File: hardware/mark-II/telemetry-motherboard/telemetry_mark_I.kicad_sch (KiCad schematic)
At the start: 78 parts, among them J1 Power, J10 5V_BUS, J11 12V_BUS, J12 24V_BUS, J13 Conn_01x02_Socket, J14 Conn_01x02_Socket, J15 Conn_01x02_Socket, J16 Conn_01x02_Socket, J17 BMS_Header, J2 PWM, J3 Analog, J4 PWM, J5 Analog, J6 Communication, J7 Digital, J8 Input_Terminal, J9 Temp_Sensor_Header, U3 LTC3114EFE-1_PBF, U4 AOZ1284PI, U5 AOZ1284PI

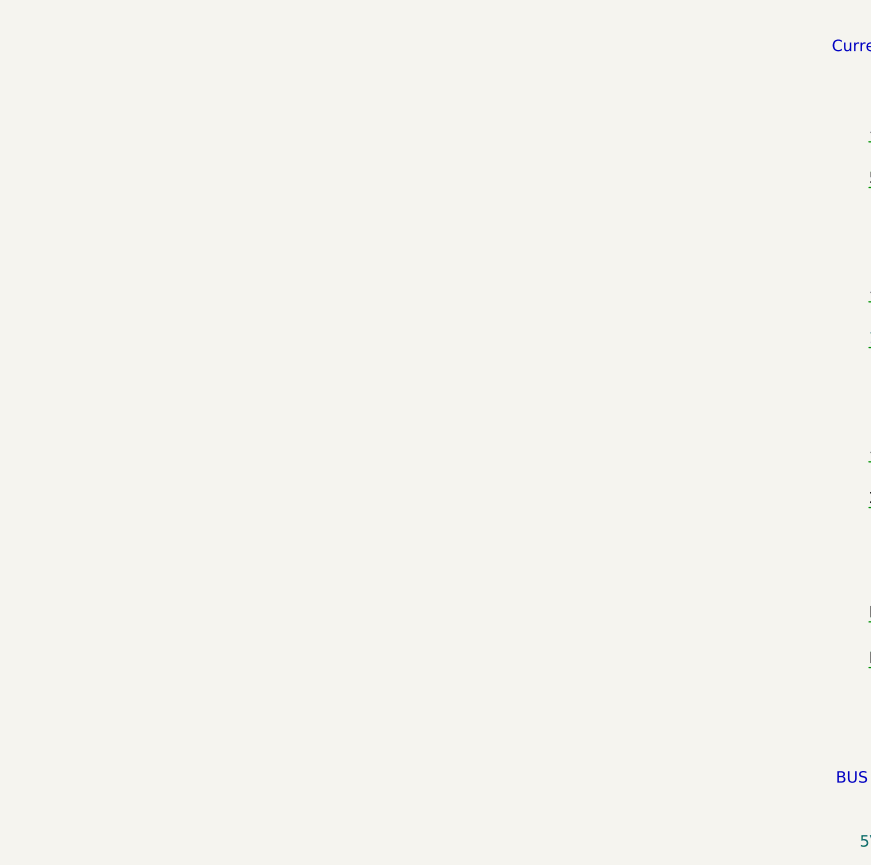
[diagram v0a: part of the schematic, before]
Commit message: Work on fault abstraction
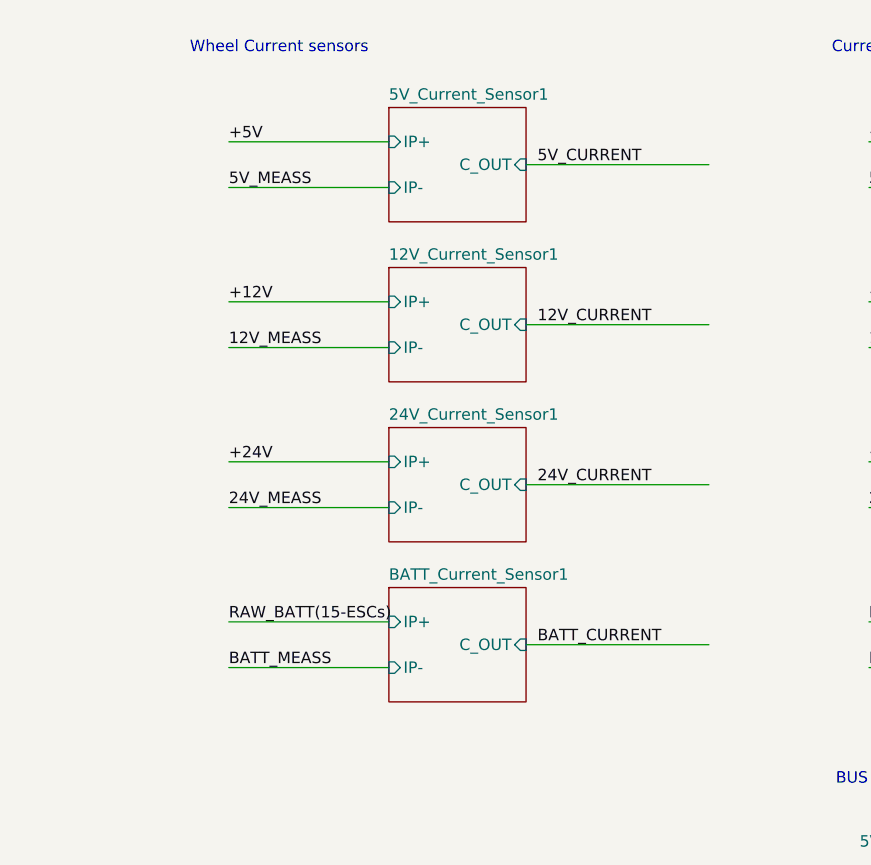
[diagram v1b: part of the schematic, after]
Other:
- added sheet 12V_Current_Sensor1 (current_sensor.kicad_sch)
- added sheet 24V_Current_Sensor1 (current_sensor.kicad_sch)
- added sheet 5V_Current_Sensor1 (current_sensor.kicad_sch)
- added sheet BATT_Current_Sensor1 (current_sensor.kicad_sch)
- note added: "Wheel Current sensors"

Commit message: New commit
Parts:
- removed C11: 30u, Capacitor_THT:CP_Radial_D5.0mm_P2.00mm, symbol Device:C_Polarized_Small_US
- removed C12, C17, C19, C27, C28: 10u, Capacitor_SMD:C_0603_1608Metric_Pad1.08x0.95mm_HandSolder, symbol Device:C_Small
- removed C14: 4.7n, Capacitor_SMD:C_0603_1608Metric_Pad1.08x0.95mm_HandSolder, symbol Device:C_Small
- removed C18, C20: 0.3n, Capacitor_SMD:C_0603_1608Metric_Pad1.08x0.95mm_HandSolder, symbol Device:C_Small
- removed C22, C23: 1n, Capacitor_SMD:C_0603_1608Metric_Pad1.08x0.95mm_HandSolder, symbol Device:C_Small
- removed C24, C25: 100n, Capacitor_SMD:C_0603_1608Metric_Pad1.08x0.95mm_HandSolder, symbol Device:C_Small
- removed C5, C6: 68n, Capacitor_SMD:C_0603_1608Metric_Pad1.08x0.95mm_HandSolder, symbol Device:C_Small
- removed C7: 33n, Capacitor_SMD:C_0603_1608Metric_Pad1.08x0.95mm_HandSolder, symbol Device:C_Small
- removed C9: 4.7u, Capacitor_SMD:C_0603_1608Metric_Pad1.08x0.95mm_HandSolder, symbol Device:C_Small
- removed D6, D7: SS54, Diode_SMD:D_SMA, symbol Device:D_Schottky
- removed J8: Input_Terminal, TerminalBlock_Ningbo-Kagnex:TerminalBlock_Ningbo-Kagnex_HB9500_1x05_P9.5mm, symbol Connector:Screw_Terminal_01x04
- removed L1: 6.8u, Inductor_SMD:L_0603_1608Metric_Pad1.05x0.95mm_HandSolder, symbol Device:L_Small
- removed L2, L3: 22u, Inductor_SMD:L_12x12mm_H8mm, symbol Device:L_Small
- removed R13: 27.4k, Resistor_SMD:R_0603_1608Metric_Pad0.98x0.95mm_HandSolder, symbol Device:R_Small_US
- removed R15: 43.2k, Resistor_SMD:R_0603_1608Metric_Pad0.98x0.95mm_HandSolder, symbol Device:R_Small_US
- removed R16, R26: 105k, Resistor_SMD:R_0603_1608Metric_Pad0.98x0.95mm_HandSolder, symbol Device:R_Small_US
- removed R17, R18: 47k, Resistor_SMD:R_0603_1608Metric_Pad0.98x0.95mm_HandSolder, symbol Device:R_Small_US
- removed R19, R21: 680k, Resistor_SMD:R_0603_1608Metric_Pad0.98x0.95mm_HandSolder, symbol Device:R_Small_US
- removed R2: 20k, Resistor_SMD:R_0603_1608Metric_Pad0.98x0.95mm_HandSolder, symbol Device:R_Small_US
- removed R20, R22: 100k, Resistor_SMD:R_0603_1608Metric_Pad0.98x0.95mm_HandSolder, symbol Device:R_Small_US
- removed R23: 52.3k, Resistor_SMD:R_0603_1608Metric_Pad0.98x0.95mm_HandSolder, symbol Device:R_Small_US
- removed R24: 10k, Resistor_SMD:R_0603_1608Metric_Pad0.98x0.95mm_HandSolder, symbol Device:R_Small_US
- removed R27: 7.5k, Resistor_SMD:R_0603_1608Metric_Pad0.98x0.95mm_HandSolder, symbol Device:R_Small_US
- removed R3: 120k, Resistor_SMD:R_0603_1608Metric_Pad0.98x0.95mm_HandSolder, symbol Device:R_Small_US
- removed R8: 2.8M, Resistor_SMD:R_0603_1608Metric_Pad0.98x0.95mm_HandSolder, symbol Device:R_Small_US
- removed U3: LTC3114EFE-1_PBF, All:SOP65P640X110-17N, symbol LTC3114EFE-1_PBF:LTC3114EFE-1_PBF
- removed U4: AOZ1284PI, Package_SO:SOIC-8-1EP_3.9x4.9mm_P1.27mm_EP2.71x3.7mm, symbol AOZ1284PI:AOZ1284PI
- removed U5: AOZ1284PI, external_symbols:SOP127P600X170-9N, symbol AOZ1284PI:AOZ1284PI
- added J18: Screw_Terminal_01x08, symbol Connector:Screw_Terminal_01x08
- J10: footprint TerminalBlock_Phoenix:TerminalBlock_Phoenix_MKDS-1,5-8_1x08_P5.00mm_Horizontal -> TerminalBlock_Phoenix:TerminalBlock_Phoenix_MKDS-1,5-8-5.08_1x08_P5.08mm_Horizontal
- J13, J14, J15, J16: footprint Connector_AMASS:AMASS_XT60-F_1x02_P7.20mm_Vertical -> Connector_AMASS:AMASS_XT60PW-F_1x02_P7.20mm_Horizontal
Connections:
- net BATT_MEASS: no longer J13.1 (Pin_1), J14.1 (Pin_1), J15.1 (Pin_1), J16.1 (Pin_1)
- net RAW_BATT(15-12): now also J18.2 (Pin_2)
- net RAW_BATT(15-24): now also J18.3 (Pin_3)
- net RAW_BATT(15-5): now also J18.1 (Pin_1)
- new net RAW_BATT(15-W1): J18.4 (Pin_4)
- new net RAW_BATT(15-W2): J18.5 (Pin_5)
- new net RAW_BATT(15-W3): J18.6 (Pin_6)
- new net RAW_BATT(15-W4): J18.7 (Pin_7)
- new net W1_MEASS: J13.1 (Pin_1)
- new net W2_MEASS: J14.1 (Pin_1)
- new net W3_MEASS: J15.1 (Pin_1)
- new net W4_MEASS: J16.1 (Pin_1)
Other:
- sheet 12V_Current_Sensor1 renamed W2_Current_Sensor
- sheet 24V_Current_Sensor1 renamed W3_Current_Sensor
- sheet 5V_Current_Sensor1 renamed W1_Current_Sensor
- sheet BATT_Current_Sensor1 renamed W4_Current_Sensor
- moved on the sheet: J10, J11, J12, J13, J14, J15, J16, J17, J9

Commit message: PDB Revised
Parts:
- removed RBOTT5, RBOTT6, RBOTT7, RBOTT8: 10K, Resistor_SMD:R_0603_1608Metric_Pad0.98x0.95mm_HandSolder, symbol Device:R_Small_US
- removed RTOP5, RTOP6, RTOP7, RTOP8: 47K, Resistor_SMD:R_0603_1608Metric_Pad0.98x0.95mm_HandSolder, symbol Device:R_Small_US
- added C5, C6, C7, C9: C_Polarized, Capacitor_SMD:CP_Elec_8x10.5, symbol Device:C_Polarized
- added J19: Conn_01x06_Pin, Connector_PinSocket_2.54mm:PinSocket_1x06_P2.54mm_Horizontal, symbol Connector:Conn_01x06_Pin
- added J20: Screw_Terminal_01x02, TerminalBlock_Phoenix:TerminalBlock_Phoenix_MKDS-1,5-2-5.08_1x02_P5.08mm_Horizontal, symbol Connector:Screw_Terminal_01x02
- added J21: Screw_Terminal_01x04, Connector_Phoenix_MC:PhoenixContact_MCV_1,5_4-GF-3.81_1x04_P3.81mm_Vertical_ThreadedFlange_MountHole, symbol Connector:Screw_Terminal_01x04
- added U1: (no value), PDB:ArduinoMega, symbol ProjectAVLibrary:ArduinoMega
- added U13: (no value), PDB:Untitled_3, symbol ProjectAVLibrary:DataLogger
- added U3: (no value), PDB:Untitled, symbol ProjectAVLibrary:5VCONVERTER
- added U4: (no value), PDB:Untitled_1, symbol ProjectAVLibrary:12VCONVERTER
- added U5: (no value), PDB:24Converter, symbol ProjectAVLibrary:24VCONVERTER
- J18: footprint (none) -> TerminalBlock_Ningbo-Kagnex:TerminalBlock_Ningbo-Kagnex_HB9500_1x08_P9.5mm
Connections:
- net GND: now also J13.1 (Pin_1), J14.1 (Pin_1), J15.1 (Pin_1), J16.1 (Pin_1), J18.1 (Pin_1), C5.2, C6.2, C7.2, C9.2; no longer J13.2 (Pin_2), J14.2 (Pin_2), J15.2 (Pin_2), J16.2 (Pin_2)
- net RAW_BATT(15-12): now also J18.5 (Pin_5); no longer J18.2 (Pin_2)
- net RAW_BATT(15-24): now also J18.6 (Pin_6); no longer J18.3 (Pin_3)
- net RAW_BATT(15-5): now also J18.4 (Pin_4); no longer J18.1 (Pin_1)
- net RAW_BATT(15-W1): now also J18.3 (Pin_3); no longer J18.4 (Pin_4)
- net RAW_BATT(15-W2): now also J18.2 (Pin_2); no longer J18.5 (Pin_5)
- net RAW_BATT(15-W3): now also J18.7 (Pin_7); no longer J18.6 (Pin_6)
- net RAW_BATT(15-W4): now also J18.8 (Pin_8); no longer J18.7 (Pin_7)
- net W1_MEASS: now also J13.2 (Pin_2), C9.1; no longer J13.1 (Pin_1)
- net W2_MEASS: now also J14.2 (Pin_2), C7.1; no longer J14.1 (Pin_1)
- net W3_MEASS: now also J15.2 (Pin_2), C6.1; no longer J15.1 (Pin_1)
- net W4_MEASS: now also J16.2 (Pin_2), C5.1; no longer J16.1 (Pin_1)
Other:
- added sheet BMS (bms.kicad_sch)
- note added: "BMS"
- note added: "Custom Symbols"
- note added: "Data Logger"
- note removed: "12V buck"
- note removed: "24V boost"
- note removed: "5V buck"
- note removed: "BMS Voltage sensors"
- moved on the sheet: J13, J14, J15, J16, J17, J9

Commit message: Added Sensors & LCD
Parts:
- J9: footprint Connector_PinHeader_2.54mm:PinHeader_1x03_P2.54mm_Vertical -> Connector_JST:JST_EH_B3B-EH-A_1x03_P2.50mm_Vertical
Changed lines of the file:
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@@
 			)
 		)
-		(property "Footprint" "Connector_PinHeader_2.54mm:PinHeader_1x03_P2.54mm_Vertical"
+		(property "Footprint" "Connector_JST:JST_EH_B3B-EH-A_1x03_P2.50mm_Vertical"
 			(at 331.47 63.5 0)
 			(hide yes)
